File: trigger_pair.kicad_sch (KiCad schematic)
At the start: 51 parts, among them J4 AudioJack2, J5 AudioJack2, J8 Conn_01x02_Pin, J9 Conn_01x02_Pin, U1 1SS362FV_L3F, U2 1SS362FV_L3F, U3 LM2902PWR, U4 1SS362FV_L3F, U5 1SS362FV_L3F, U6 1SS362FV_L3F, U7 1SS362FV_L3F

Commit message: Initial layout
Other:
- moved on the sheet: C10, C11, C12, C13, C14, C7, C8, C9, J5, J8, J9, R13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

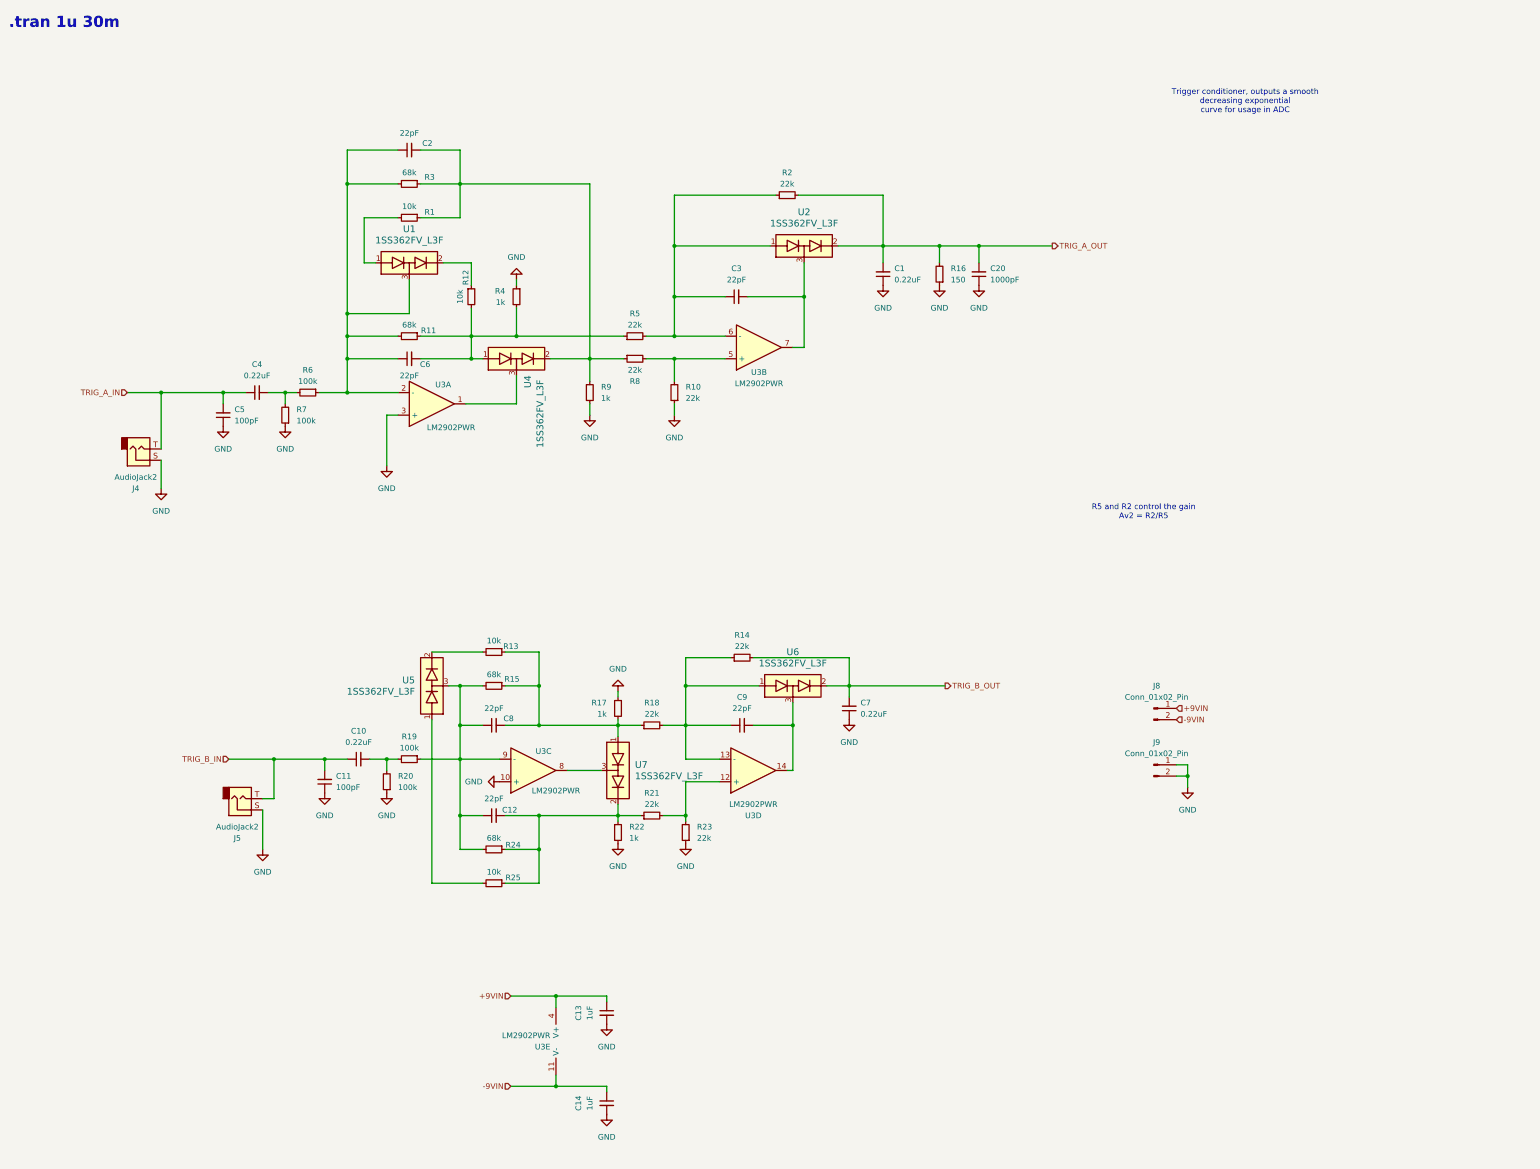
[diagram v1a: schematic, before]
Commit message: Double trigger layout to test
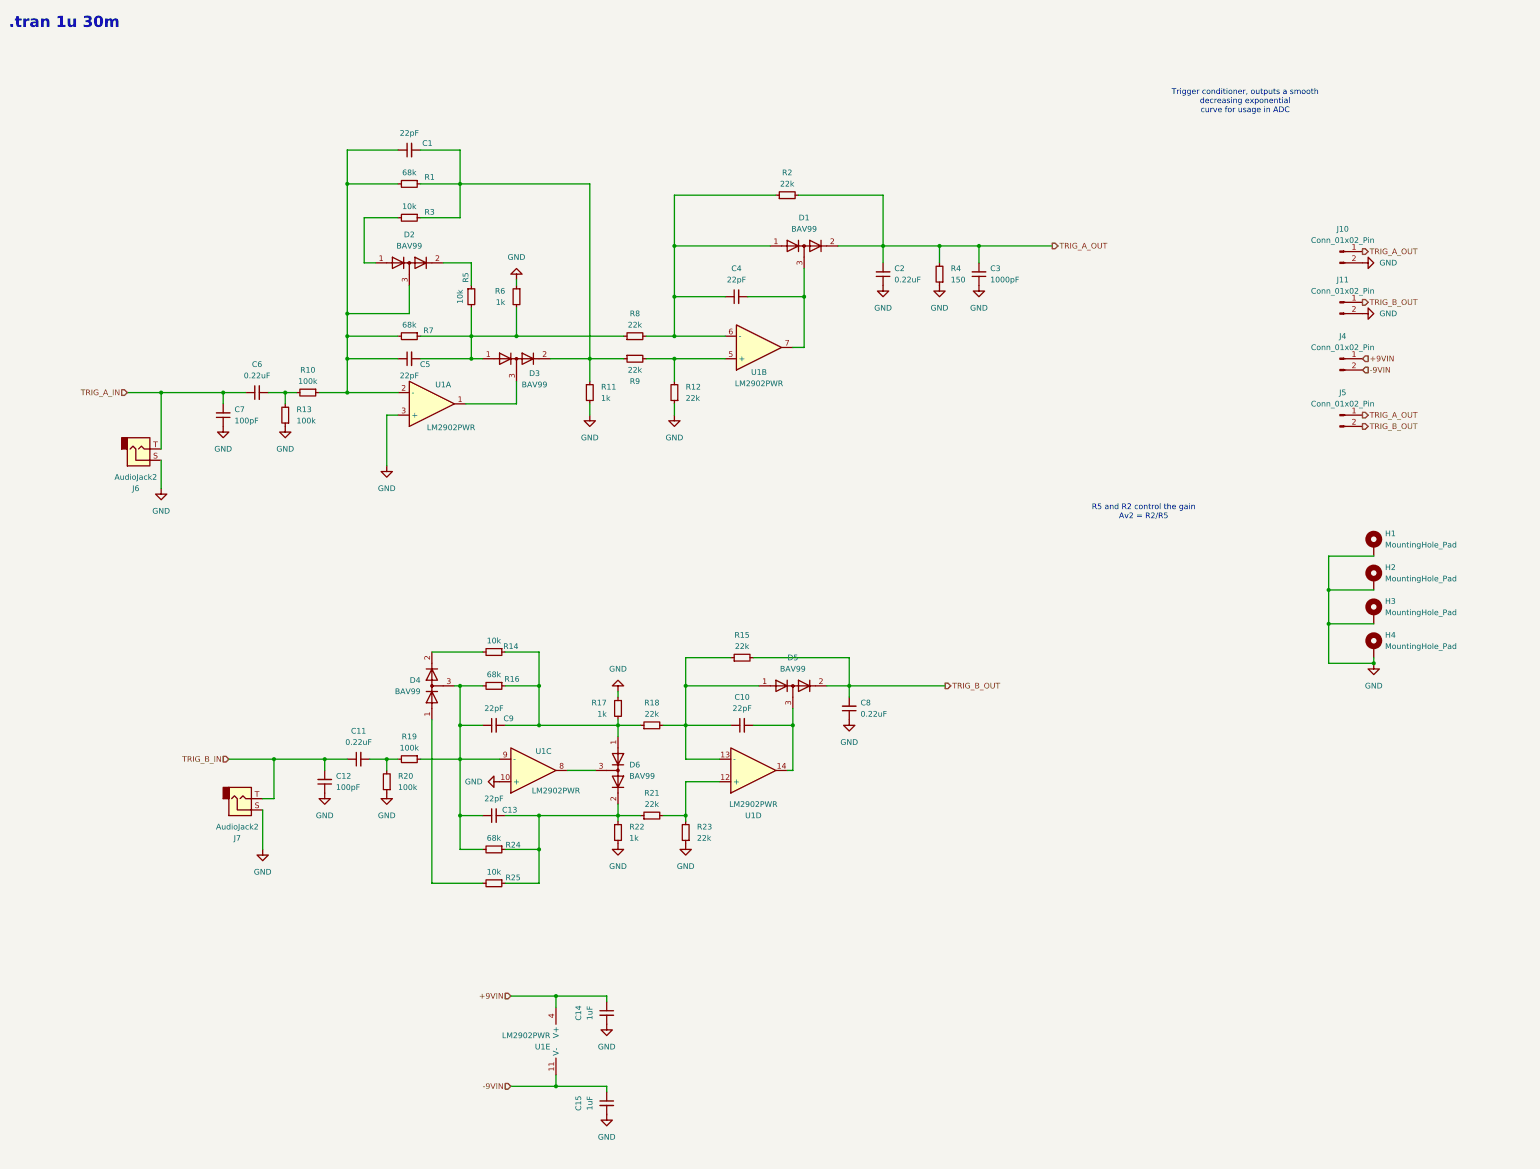
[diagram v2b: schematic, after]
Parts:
- removed J9: Conn_01x02_Pin, Connector_JST:JST_PH_B2B-PH-K_1x02_P2.00mm_Vertical, symbol Connector:Conn_01x02_Pin
- removed U1, U2, U4, U5, U6, U7: 1SS362FV_L3F, mod:DIODE_1SS362FV, symbol DIODE_SET_1SS362FV:1SS362FV_L3F
- added D1, D2, D3, D4, D5, D6: BAV99, Package_TO_SOT_SMD:SOT-23, symbol Diode:BAV99
- added H1, H2, H3, H4: MountingHole_Pad, MountingHole:MountingHole_2.2mm_M2_Pad_Via, symbol Mechanical:MountingHole_Pad
- added J10, J11: Conn_01x02_Pin, Connector_PinHeader_2.54mm:PinHeader_1x02_P2.54mm_Vertical, symbol Connector:Conn_01x02_Pin
- added J5: Conn_01x02_Pin, Connector_JST:JST_PH_B2B-PH-K_1x02_P2.00mm_Vertical, symbol Connector:Conn_01x02_Pin
- C1: renamed from C2; footprint Capacitor_SMD:C_0402_1005Metric -> C_0402_custom:C_0402_1005Metric
- C10: renamed from C9; footprint Capacitor_SMD:C_0402_1005Metric -> C_0402_custom:C_0402_1005Metric
- C13: renamed from C12; footprint Capacitor_SMD:C_0402_1005Metric -> C_0402_custom:C_0402_1005Metric
- C4: renamed from C3; footprint Capacitor_SMD:C_0402_1005Metric -> C_0402_custom:C_0402_1005Metric
- C5: renamed from C6; footprint Capacitor_SMD:C_0402_1005Metric -> C_0402_custom:C_0402_1005Metric
- C9: renamed from C8; footprint Capacitor_SMD:C_0402_1005Metric -> C_0402_custom:C_0402_1005Metric
- R1: renamed from R3; footprint Resistor_SMD:R_0402_1005Metric -> R_0402_custom:R_0402_1005Metric
- R11: renamed from R9; footprint Resistor_SMD:R_0402_1005Metric -> R_0402_custom:R_0402_1005Metric
- R12: renamed from R10; footprint Resistor_SMD:R_0402_1005Metric -> R_0402_custom:R_0402_1005Metric
- R14: renamed from R13; footprint Resistor_SMD:R_0402_1005Metric -> R_0402_custom:R_0402_1005Metric
- R15: renamed from R14; footprint Resistor_SMD:R_0402_1005Metric -> R_0402_custom:R_0402_1005Metric
- R16: renamed from R15; footprint Resistor_SMD:R_0402_1005Metric -> R_0402_custom:R_0402_1005Metric
- R17, R18, R2, R21, R22, R23, R24, R25: footprint Resistor_SMD:R_0402_1005Metric -> R_0402_custom:R_0402_1005Metric
- R3: renamed from R1; footprint Resistor_SMD:R_0402_1005Metric -> R_0402_custom:R_0402_1005Metric
- R4: renamed from R16; footprint Resistor_SMD:R_0402_1005Metric -> R_0402_custom:R_0402_1005Metric
- R5: renamed from R12; footprint Resistor_SMD:R_0402_1005Metric -> R_0402_custom:R_0402_1005Metric
- R6: renamed from R4; footprint Resistor_SMD:R_0402_1005Metric -> R_0402_custom:R_0402_1005Metric
- R7: renamed from R11; footprint Resistor_SMD:R_0402_1005Metric -> R_0402_custom:R_0402_1005Metric
- R8: renamed from R5; footprint Resistor_SMD:R_0402_1005Metric -> R_0402_custom:R_0402_1005Metric
- R9: renamed from R8; footprint Resistor_SMD:R_0402_1005Metric -> R_0402_custom:R_0402_1005Metric
- renumbered C10 to C11, C11 to C12, C13 to C14, C14 to C15, C1 to C2, C20 to C3, C4 to C6, C5 to C7, C7 to C8, J8 to J4, J4 to J6, J5 to J7, R6 to R10, R7 to R13, U3 to U1
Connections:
- net GND: now also H1.1, H2.1, H3.1, H4.1, J10.2 (Pin_2), J11.2 (Pin_2)
- net TRIG_A_OUT: now also D1.2 (A), J10.1 (Pin_1), J5.1 (Pin_1)
- net TRIG_B_OUT: now also D5.2 (A), J11.1 (Pin_1), J5.2 (Pin_2)
- net at C5.2, R5.2, R6.2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: now also D3.1 (K)
- net at C1.1, C5.1, R1.2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: now also D2.3 (K)
- net at R3.2: now also D2.1 (K)
- net at R5.1: now also D2.2 (A)
- net at C1.2, R1.1, R11.1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: now also D3.2 (A)
- net at C9.2, R14.1, R16.1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: now also D6.1 (K)
- net at C13.2, R21.1, R22.1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: now also D6.2 (A)
- net at U1.8: now also D6.3 (K)
- net at C4.1, R2.1, R8.2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: now also D1.1 (K)
- net at C10.1, R15.1, R18.2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: now also D5.1 (K)
- net at C10.2, U1.14: now also D5.3 (K)
- net at C13.1, C9.1, R16.2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: now also D4.3 (K)
- net at U1.1: now also D3.3 (K)
- net at C4.2, U1.7: now also D1.3 (K)
- net at R25.2: now also D4.1 (K)
- net at R14.2: now also D4.2 (A)
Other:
- moved on the sheet: J4

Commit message: Production ready pcb
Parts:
- added D7: LED, LED_SMD:LED_0805_2012Metric, symbol Device:LED
- added R59: 1.5k, Resistor_SMD:R_0603_1608Metric, symbol Device:R_Small
- added R60: 100, R_0402_custom:R_0402_1005Metric, symbol Device:R_Small
- C1, C10, C13, C4, C5, C9: LTSC (none) -> C1555
- C11, C2, C6, C8: LTSC (none) -> C21120
- C12, C7: LTSC (none) -> C14858
- C14, C15: LTSC (none) -> C15849
- C3: LTSC (none) -> C1588
- D1, D2, D3, D4, D5, D6: LTSC (none) -> C2500
- J10, J11, J4, J5, J6, J7: now not fitted; now left out of the parts list
- R1, R16, R24, R7: footprint R_0402_custom:R_0402_1005Metric -> Resistor_SMD:R_0603_1608Metric; LTSC (none) -> C23231
- R10, R13, R19, R20: LTSC (none) -> C25803
- R11, R17, R22, R6: LTSC (none) -> C11702
- R12, R15, R18, R2, R21, R23, R8, R9: LTSC (none) -> C25768
- R14, R25, R3, R5: LTSC (none) -> C25744
- R4: value 150 -> 100; LTSC (none) -> C25076
- U1: LTSC (none) -> C71035
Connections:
- net +9VIN: now also R59.1
- net GND: now also D7.1 (K)
- net TRIG_A_OUT: now also R60.2; no longer C2.2, D1.2 (A), R2.2
- new net: C2.2, D1.2 (A), R2.2, R60.1
- new net: D7.2 (A), R59.2

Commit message: Minor upates to the pcb
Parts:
- added FB3, FB4: FerriteBead_Small, Inductor_SMD:L_0805_2012Metric, symbol Device:FerriteBead_Small
- C1, C10, C13, C4, C5, C9: LCSC (none) -> C1555; LTSC C1555 -> (none)
- C11, C2, C6, C8: value 0.22uF -> 220nF; LCSC (none) -> C21120; LTSC C21120 -> (none)
- C12, C7: LCSC (none) -> C14858; LTSC C14858 -> (none)
- C14, C15: LCSC (none) -> C15849; LTSC C15849 -> (none)
- C3: value 1000pF -> 1nF; LCSC (none) -> C1588; LTSC C1588 -> (none)
- D1, D2, D3, D4, D5, D6: value BAV99 -> BAV99,215; LCSC (none) -> C2500; LTSC C2500 -> (none)
- D7: value LED -> KT-0805G; LCSC (none) -> C2297; LTSC C2297 -> (none)
- J10, J11, J4, J5, J6, J7: now fitted
- R1, R16, R24, R7: LCSC (none) -> C23231; LTSC C23231 -> (none)
- R10, R13, R19, R20: LCSC (none) -> C25803; LTSC C25803 -> (none)
- R11, R17, R22, R6: LCSC (none) -> C11702; LTSC C11702 -> (none)
- R12, R15, R18, R2, R21, R23, R8, R9: LCSC (none) -> C25768; LTSC C25768 -> (none)
- R14, R25, R3, R5: LCSC (none) -> C25744; LTSC C25744 -> (none)
- R4, R60: LCSC (none) -> C25076; LTSC C25076 -> (none)
- R59: LCSC (none) -> C22843; LTSC C22843 -> (none)
- U1: LCSC (none) -> C71035; LTSC C71035 -> (none)
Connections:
- net TRIG_A_IN: now also FB3.1; no longer C6.1, C7.2
- net TRIG_B_IN: now also FB4.1; no longer C11.1, C12.2
- new net: C11.1, C12.2, FB4.2
- new net: C6.1, C7.2, FB3.2

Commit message: Simulation fixes + board fixes
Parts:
- removed J4, J5: Conn_01x02_Pin, Connector_JST:JST_PH_B2B-PH-K_1x02_P2.00mm_Vertical, symbol Connector:Conn_01x02_Pin
- removed R4, R60: 100, R_0402_custom:R_0402_1005Metric, symbol Device:R_Small
- added J12, J4: Conn_01x03_Pin, Connector_JST:JST_PH_B3B-PH-K_1x03_P2.00mm_Vertical, symbol Connector:Conn_01x03_Pin
- added J13: TRIG_B_SIG, symbol Connector:Conn_01x01_Pin
- added J5: TRIG_A_SIG, symbol Connector:Conn_01x01_Pin
- FB3, FB4: value FerriteBead_Small -> 600
- U1: value LM2902PWR -> LM324DT
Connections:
- net +9VIN: now also J12.1 (Pin_1)
- net -9VIN: now also J12.3 (Pin_3)
- net GND: now also J12.2 (Pin_2), J4.3 (Pin_3)
- net TRIG_A_IN: now also J5.1 (Pin_1)
- net TRIG_A_OUT: now also C2.2, D1.2 (A), R2.2, J4.1 (Pin_1)
- net TRIG_B_IN: now also J13.1 (Pin_1)
- net TRIG_B_OUT: now also J4.2 (Pin_2)
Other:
- note added: ".tran 1u 60m"
- note removed: ".tran 1u 30m"
- note removed: "R5 and R2 control the gain Av2 = R2/R5"
- moved on the sheet: C10, C11, C12, C13, C14, C15, C8, C9, D4, D5, D6, D7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

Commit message: Add channels
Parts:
- removed D7: KT-0805G, LED_SMD:LED_0805_2012Metric, symbol Device:LED
- removed H1, H2, H3, H4: MountingHole_Pad, MountingHole:MountingHole_2.2mm_M2_Pad_Via, symbol Mechanical:MountingHole_Pad
- removed J10, J11: Conn_01x02_Pin, Connector_PinHeader_2.54mm:PinHeader_1x02_P2.54mm_Vertical, symbol Connector:Conn_01x02_Pin
- removed J12, J4: Conn_01x03_Pin, Connector_JST:JST_PH_B3B-PH-K_1x03_P2.00mm_Vertical, symbol Connector:Conn_01x03_Pin
- removed R59: 1.5k, Resistor_SMD:R_0603_1608Metric, symbol Device:R_Small
- added C12: 1nF, Capacitor_SMD:C_0603_1608Metric, symbol Device:C_Small
- renumbered C9 to C10, C8 to C11, C10 to C13, C13 to C14, C11 to C15, C12 to C16, C14 to C7, C7 to C8, C15 to C9, D1 to D3, D3 to D4, D4 to D5, D5 to D6, D6 to D7, FB3 to FB1, FB4 to FB2, J5 to J6, J6 to J7, J13 to J8, J7 to J9, R16 to R14, R14 to R15, R15 to R16, R25 to R17, R17 to R18, R24 to R19, R1 to R2, R18 to R20, R19 to R22, R22 to R23, R23 to R24, R20 to R25, R2 to R4
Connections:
- net GND: now also C12.1
- net TRIG_B_OUT: now also C12.2
- net at C10.1, D5.3 (K), R14.2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: now also C14.2; no longer C14.1
- net at C10.2, R14.1, R15.1: now also D7.2 (A), R21.1, R23.1; no longer D7.1 (K), R18.2, R20.1
- net at R17.2: now also C14.1, D7.1 (K), R18.2, R19.1, R20.1; no longer D5.1 (K)
- net at D5.2 (A): now also R17.1; no longer R15.2
- new net: D5.1 (K), R15.2
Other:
- note removed: ".tran 1u 60m"
- moved on the sheet: C1, C10, C11, C13, C14, C15, C16, C2, C3, C4, C5, C6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
